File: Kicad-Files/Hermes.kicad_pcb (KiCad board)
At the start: 2 copper layers, 67.9 x 40.1 mm, 14 parts, among them J1 Conn_01x04_Socket, J2 Conn_01x01_Pin, J3 Conn_01x01_Pin, U1 XIAO-RP2040-DIP, U2 VL53L1CXV0FY1

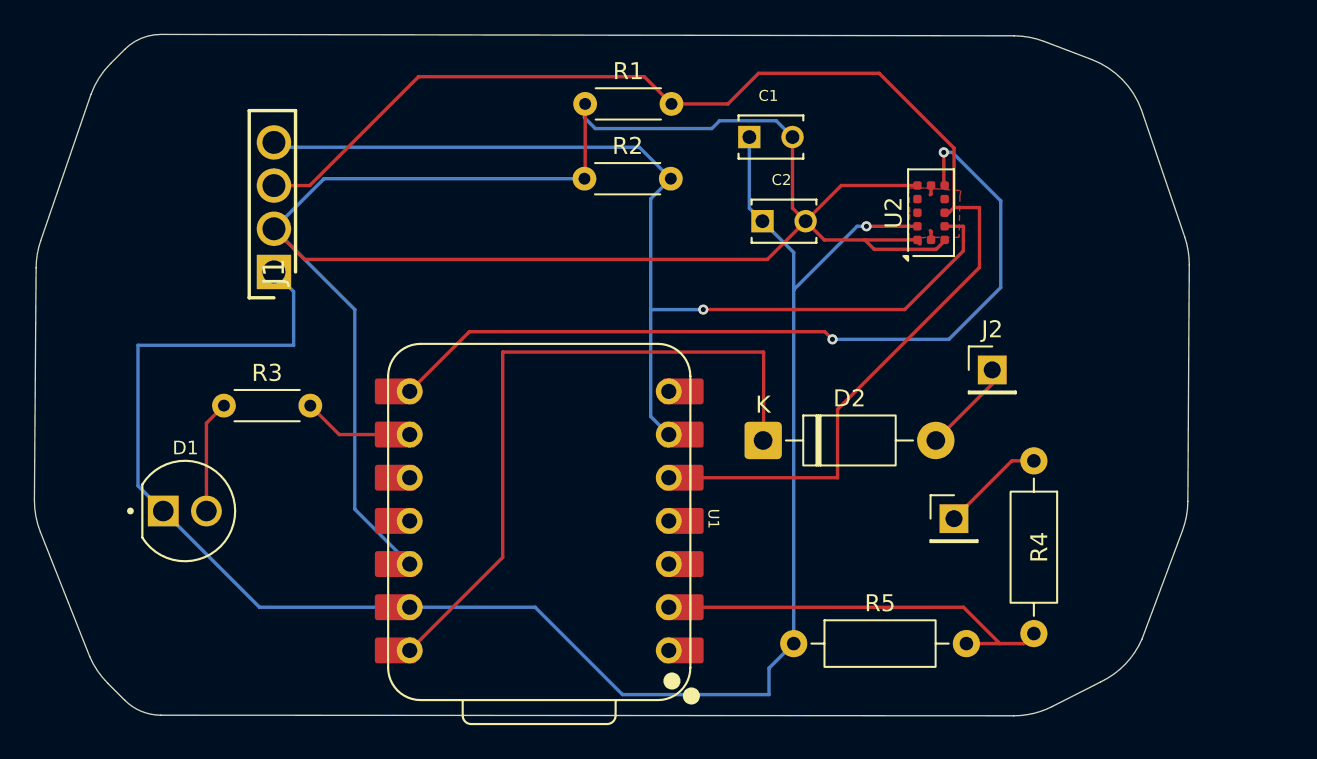
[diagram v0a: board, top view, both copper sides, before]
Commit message: Fix BOM update files and add a button to the pcb
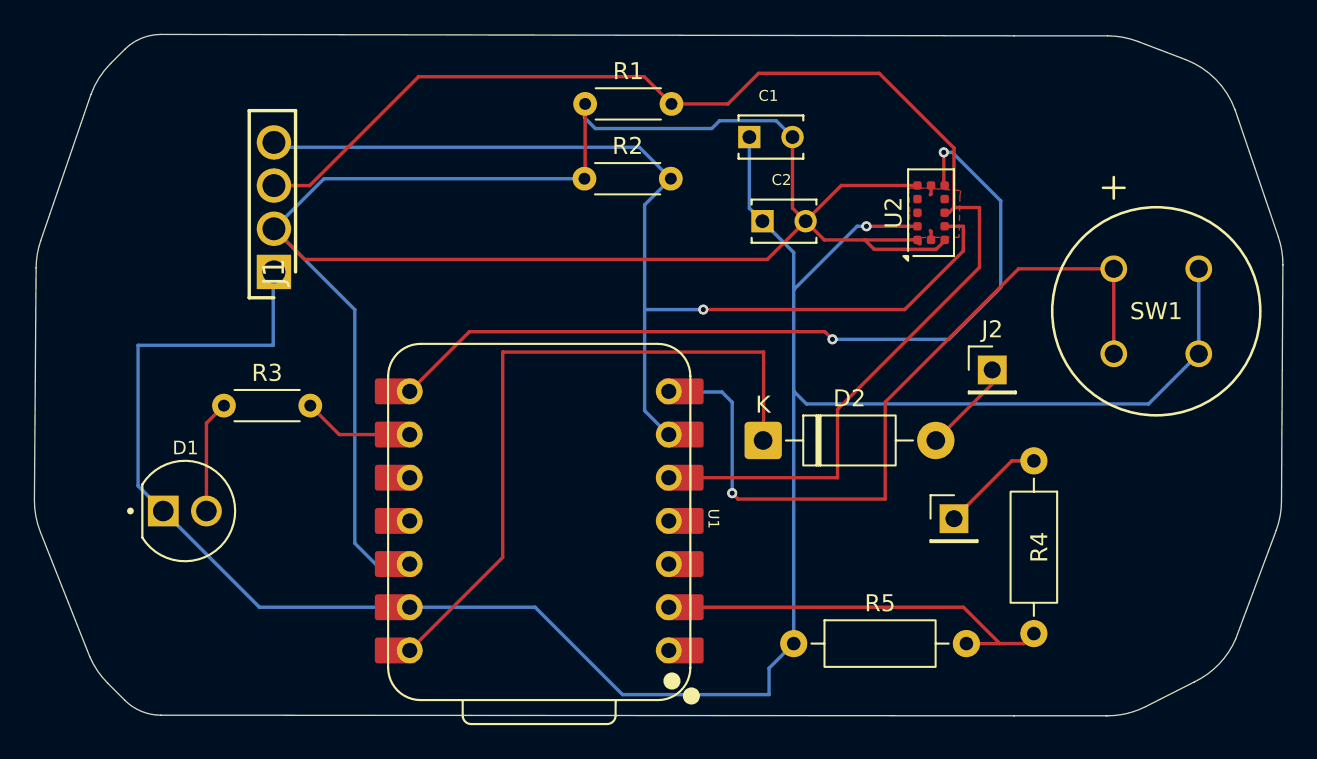
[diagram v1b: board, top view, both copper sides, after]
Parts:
- added SW1: D6R90F2LFS, footprints:D6R90_CNK, F.Cu at (167.9, 133.5)
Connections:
- U1 pad 7: unconnected-(U1-P0_D6_TX-Pad7)_1 -> Button
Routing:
- net Button: track 0.00 -> 45.9 mm, vias 0 -> 1
- net GND: track 108.9 -> 137.6 mm
- net 3V3: track 118.8 -> 119.9 mm
- net SCL: track 62.6 -> 63.2 mm
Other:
- board size 67.9 x 40.1 mm -> 73.4 x 40.1 mm
